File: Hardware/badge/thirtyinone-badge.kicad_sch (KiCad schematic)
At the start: 29 parts, among them J1 SWD, J2 TagConnect, J3 OLED, J4 USB3140-30-0170-1-C, J5 uC Interface, SW1 Power, U1 MIC5219-3.6YM5, U2 ATSAMD21G15A-A

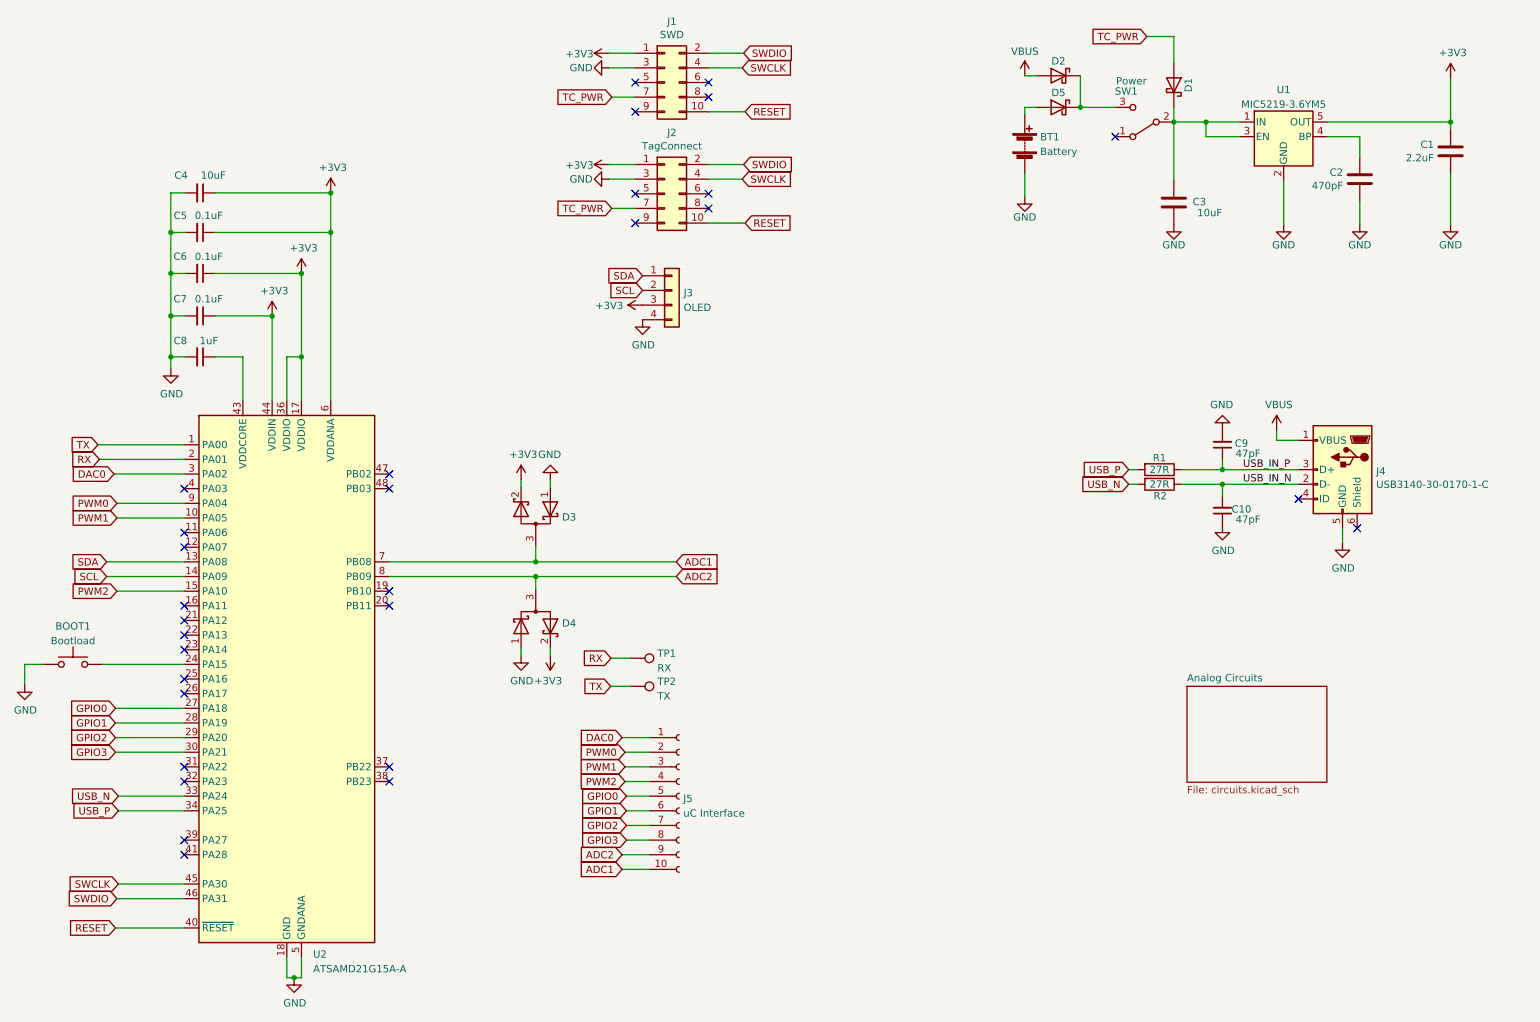
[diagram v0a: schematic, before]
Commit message: Updated to hardware version 1.1 to reflect some footprint fixes, and swap to an alternate microcontroller due to parts availability
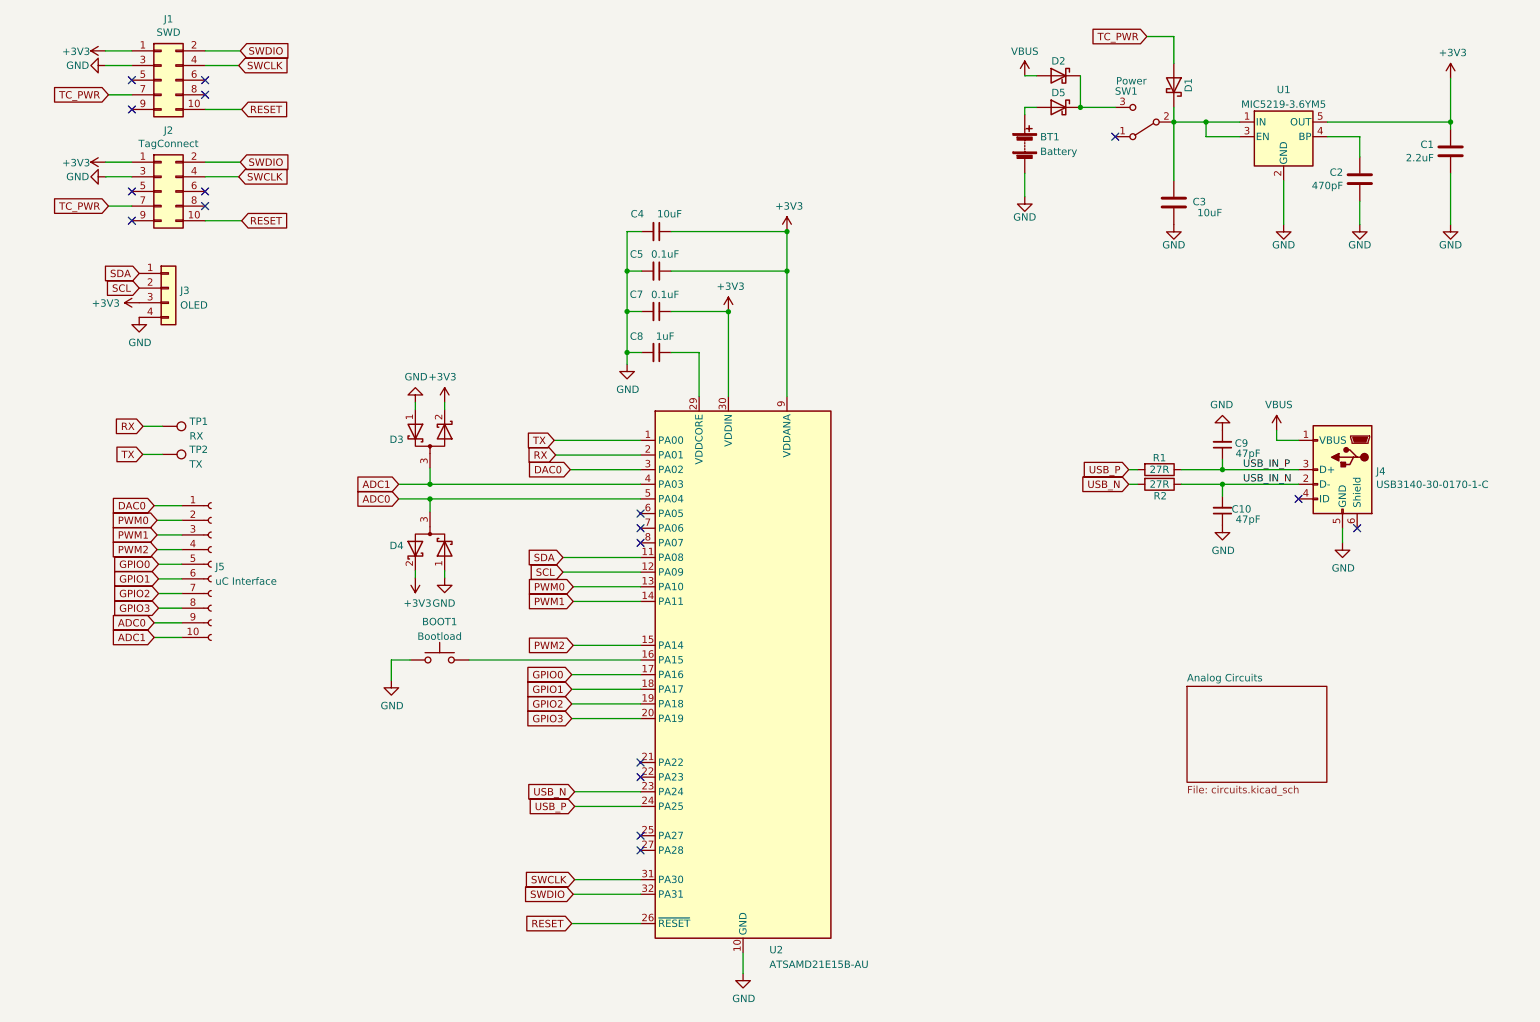
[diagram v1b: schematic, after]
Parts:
- removed C6: 0.1uF, Capacitor_SMD:C_0603_1608Metric, symbol Device:C_Small
- BOOT1: footprint Button_Switch_SMD:SW_Push_1P1T_NO_6x6mm_H9.5mm -> lib_fp:SW_Push_1P1T_NO_CK_PTS526
- D3, D4: footprint Package_TO_SOT_SMD:SOT-323_SC-70 -> Package_TO_SOT_SMD:SOT-23
- U2: value ATSAMD21G15A-A -> ATSAMD21E15B-AU; footprint Package_QFP:TQFP-48_7x7mm_P0.5mm -> Package_QFP:TQFP-32_7x7mm_P0.8mm; symbol MCU_Microchip_SAMD:ATSAMD21G15A-A -> MCU_Microchip_SAMD:ATSAMD21E15B-A
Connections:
- net +3V3: now also U2.30 (VDDIN), U2.9 (VDDANA); no longer U2.17 (VDDIO), U2.36 (VDDIO), U2.44 (VDDIN), U2.6 (VDDANA)
- net ADC1: now also U2.4 (PA03); no longer U2.7 (PB08)
- net GND: now also U2.10 (GND), U2.28 (GND); no longer U2.18 (GND), U2.35 (GND), U2.42 (GND), U2.5 (GNDANA)
- net GPIO0: now also U2.17 (PA16); no longer U2.27 (PA18)
- net GPIO1: now also U2.18 (PA17); no longer U2.28 (PA19)
- net GPIO2: now also U2.19 (PA18); no longer U2.29 (PA20)
- net GPIO3: now also U2.20 (PA19); no longer U2.30 (PA21)
- net PWM0: now also U2.13 (PA10); no longer U2.9 (PA04)
- net PWM1: now also U2.14 (PA11); no longer U2.10 (PA05)
- net RESET: now also U2.26 (~{RESET}); no longer U2.40 (~{RESET})
- net SCL: now also U2.12 (PA09); no longer U2.14 (PA09)
- net SDA: now also U2.11 (PA08); no longer U2.13 (PA08)
- net SWCLK: now also U2.31 (PA30); no longer U2.45 (PA30)
- net SWDIO: now also U2.32 (PA31); no longer U2.46 (PA31)
- net USB_N: now also U2.23 (PA24); no longer U2.33 (PA24)
- net USB_P: now also U2.24 (PA25); no longer U2.34 (PA25)
- net at BOOT1.2: now also U2.16 (PA15); no longer U2.24 (PA15)
- net at C8.1: now also U2.29 (VDDCORE); no longer U2.43 (VDDCORE)
- net ADC2 renamed ADC0
- net ADC0: now also U2.5 (PA04); no longer U2.8 (PB09)
- no-connect marks 30 -> 18
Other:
- moved on the sheet: BOOT1, C4, C5, C7, C8, D3, D4, J1, J2, J3, J5, TP1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
